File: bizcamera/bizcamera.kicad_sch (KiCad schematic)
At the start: 1 part

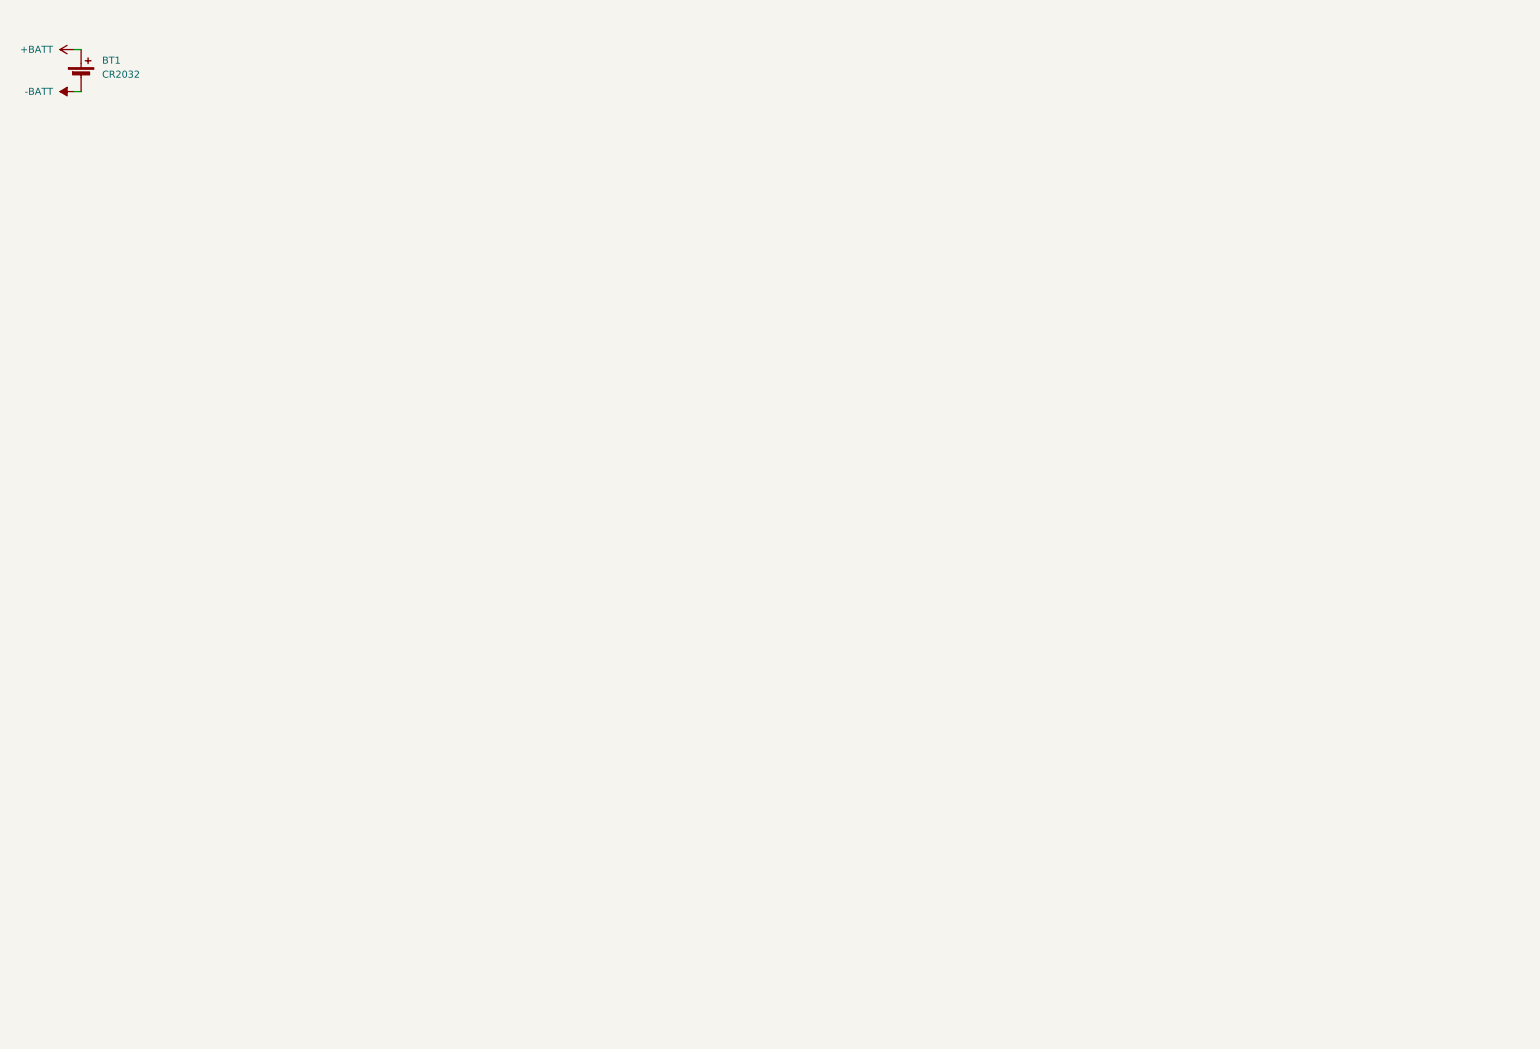
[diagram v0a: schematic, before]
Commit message: Schematic rev1
Rev1 of the schematic, not finished, but close.

Switched to rp2350 because PIO is powerful enough to grab frames without DCMI iface
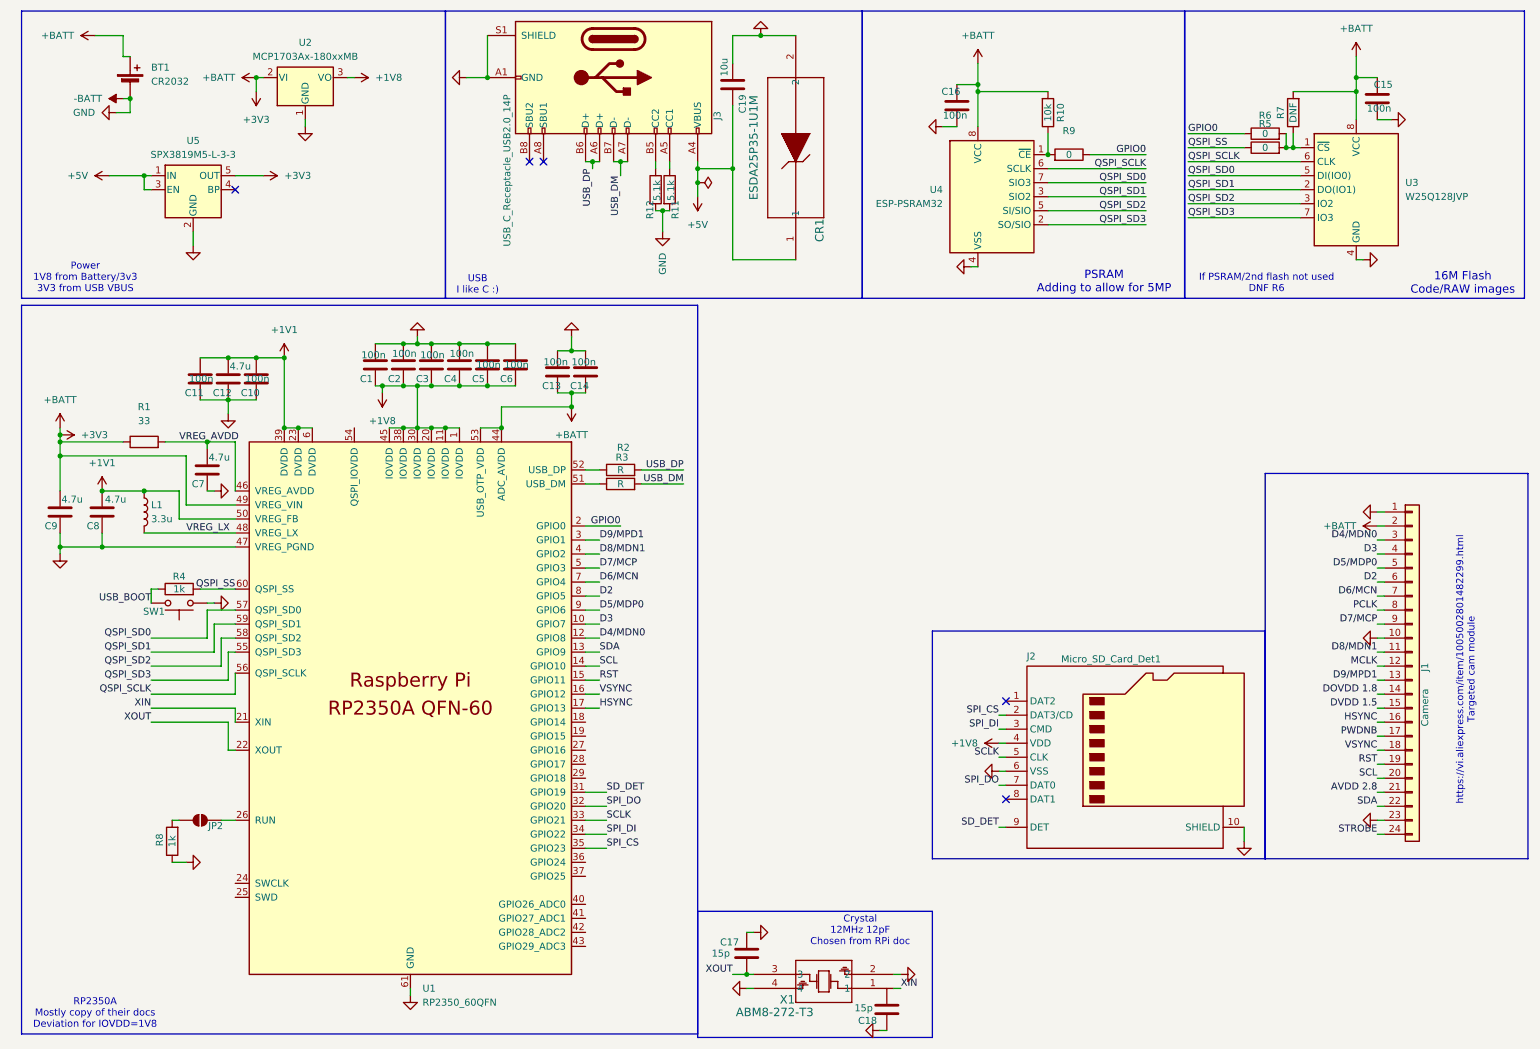
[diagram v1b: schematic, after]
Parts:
- added C1, C10, C11, C13, C14, C15, C16, C2, C3, C4, C5, C6: 100n, Capacitor_SMD:C_0402_1005Metric, symbol Device:C
- added C12, C7, C8, C9: 4.7u, Capacitor_SMD:C_0402_1005Metric, symbol Device:C
- added C17, C18: 15p, Capacitor_SMD:C_0402_1005Metric, symbol Device:C
- added C19: 10u, Capacitor_SMD:C_0603_1608Metric, symbol Device:C
- added CR1: ESDA25P35-1U1M, lib:QFN1610_STM-M, symbol ESDA25P35:ESDA25P35-1U1M
- added J1: Camera, Connector_FFC-FPC:Hirose_FH12-24S-0.5SH_1x24-1MP_P0.50mm_Horizontal, symbol Connector_Generic:Conn_01x24
- added J2: Micro_SD_Card_Det1, Connector_Card:microSD_HC_Hirose_DM3D-SF, symbol Connector:Micro_SD_Card_Det1
- added J3: USB_C_Receptacle_USB2.0_14P, Connector_USB:USB_C_Receptacle_HCTL_HC-TYPE-C-16P-01A, symbol Connector:USB_C_Receptacle_USB2.0_16P
- added JP2: USB_BOOT, Jumper:SolderJumper-2_P1.3mm_Open_RoundedPad1.0x1.5mm, symbol Jumper:SolderJumper_2_Open
- added L1: 3.3u, symbol Device:L
- added R1: 33, Resistor_SMD:R_0402_1005Metric, symbol Device:R
- added R10: 10k, Resistor_SMD:R_0402_1005Metric, symbol Device:R
- added R11, R12: 5.1k, Resistor_SMD:R_0603_1608Metric, symbol Device:R
- added R2, R3: R, Resistor_SMD:R_0402_1005Metric, symbol Device:R
- added R4, R8: 1k, Resistor_SMD:R_0402_1005Metric, symbol Device:R
- added R5, R6, R9: 0, Resistor_SMD:R_0402_1005Metric, symbol Device:R
- added R7: DNF, Resistor_SMD:R_0402_1005Metric, symbol Device:R
- added SW1: USB_BOOT, symbol Switch:SW_Push
- added U1: RP2350_60QFN, RP2350A:RP2350-QFN-60-1EP_7x7_P0.4mm_EP3.4x3.4mm_ThermalVias, symbol RP2350A:RP2350_60QFN
- added U2: MCP1703Ax-180xxMB, Package_TO_SOT_SMD:SOT-89-3, symbol Regulator_Linear:MCP1703Ax-180xxMB
- added U3: W25Q128JVP, Package_SON:WSON-8-1EP_6x5mm_P1.27mm_EP3.4x4.3mm, symbol Memory_Flash:W25Q128JVP
- added U4: ESP-PSRAM32, Package_SO:SOIC-8_3.9x4.9mm_P1.27mm, symbol Memory_RAM:ESP-PSRAM32
- added U5: SPX3819M5-L-3-3, Package_TO_SOT_SMD:SOT-23-5, symbol Regulator_Linear:SPX3819M5-L-3-3
- added X1: ABM8-272-T3, symbol ABM8-272-T3:ABM8-272-T3
- BT1: footprint (none) -> Battery:BatteryHolder_Keystone_3009_1x2450
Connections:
- net -BATT: now also C1.1, C10.2, C11.2, C12.2, C13.1, C14.1, C15.1, C16.1, C17.2, C18.2, C19.2, C2.1, C3.1, C4.1, C5.1, C6.1, C7.2, C8.2, C9.2, CR1.2, J1.1 (Pin_1), J1.10 (Pin_10), J1.23 (Pin_23), J2.10 (SHIELD), J2.6 (VSS), J3.A1 (GND), J3.A12 (GND), J3.B1 (GND), J3.B12 (GND), J3.S1 (SHIELD), R11.2, R12.2, R8.1, SW1.1, U1.47 (VREG_PGND), U1.61 (GND), U2.1 (GND), U3.4 (GND), U4.4 (VSS), U5.2 (GND), X1.2, X1.4
- net +BATT renamed +3V3
- net +3V3: now also C13.2, C14.2, C15.2, C16.2, C9.1, J1.2 (Pin_2), R1.1, R10.2, R7.2, U1.44 (ADC_AVDD), U1.49 (VREG_VIN), U1.53 (USB_OTP_VDD), U2.2 (VI), U3.8 (VCC), U4.8 (VCC), U5.5 (OUT)
- new net: R10.1, R9.2, U4.1 (~{CE})
- new net: R5.2, R6.2, R7.1, U3.1 (~{CS})
- new net: J3.A5 (CC1), R11.1
- new net: J3.B5 (CC2), R12.1
- new net: JP2.2 (B), R8.2
- new net: R3.1, U1.51 (USB_DM)
- new net: JP2.1 (A), U1.26 (RUN)
- new net: R2.1, U1.52 (USB_DP)
- new net +1V1: C10.1, C11.1, C12.1, C8.1, L1.1, U1.23 (DVDD), U1.39 (DVDD), U1.50 (VREG_FB), U1.6 (DVDD)
- new net +1V8: C1.2, C2.2, C3.2, C4.2, C5.2, C6.2, J2.4 (VDD), U1.1 (IOVDD), U1.11 (IOVDD), U1.20 (IOVDD), U1.30 (IOVDD), U1.38 (IOVDD), U1.45 (IOVDD), U2.3 (VO)
- new net +5V: C19.1, CR1.1, J3.A4 (VBUS), J3.A9 (VBUS), J3.B4 (VBUS), J3.B9 (VBUS), U5.1 (IN), U5.3 (EN)
- new net AVDD 2.8: J1.21 (Pin_21)
- new net D2: J1.6 (Pin_6), U1.8 (GPIO5)
- new net D3: J1.4 (Pin_4), U1.10 (GPIO7)
- new net D4/MDN0: J1.3 (Pin_3), U1.12 (GPIO8)
- new net D5/MDP0: J1.5 (Pin_5), U1.9 (GPIO6)
- new net D6/MCN: J1.7 (Pin_7), U1.7 (GPIO4)
- new net D7/MCP: J1.9 (Pin_9), U1.5 (GPIO3)
- new net D8/MDN1: J1.11 (Pin_11), U1.4 (GPIO2)
- new net D9/MPD1: J1.13 (Pin_13), U1.3 (GPIO1)
- new net DOVDD 1.8: J1.14 (Pin_14)
- new net DVDD 1.5: J1.15 (Pin_15)
- new net GPIO0: R6.1, R9.1, U1.2 (GPIO0)
- new net HSYNC: J1.16 (Pin_16), U1.17 (GPIO13)
- new net MCLK: J1.12 (Pin_12)
- new net PCLK: J1.8 (Pin_8)
- new net PWDNB: J1.17 (Pin_17)
- new net QSPI_SCLK: U1.56 (QSPI_SCLK), U3.6 (CLK), U4.6 (SCLK)
- new net QSPI_SD0: U1.57 (QSPI_SD0), U3.5 (DI(IO0)), U4.7 (SIO3)
- new net QSPI_SD1: U1.59 (QSPI_SD1), U3.2 (DO(IO1)), U4.3 (SIO2)
- new net QSPI_SD2: U1.58 (QSPI_SD2), U3.3 (IO2), U4.5 (SI/SIO)
- new net QSPI_SD3: U1.55 (QSPI_SD3), U3.7 (IO3), U4.2 (SO/SIO)
- new net QSPI_SS: R4.2, R5.1, U1.60 (QSPI_SS)
- new net RST: J1.19 (Pin_19), U1.15 (GPIO11)
- new net SCL: J1.20 (Pin_20), U1.14 (GPIO10)
- new net SCLK: J2.5 (CLK), U1.33 (GPIO21)
- new net SDA: J1.22 (Pin_22), U1.13 (GPIO9)
- new net SD_DET: J2.9 (DET), U1.31 (GPIO19)
- new net SPI_CS: J2.2 (DAT3/CD), U1.35 (GPIO23)
- new net SPI_DI: J2.3 (CMD), U1.34 (GPIO22)
- new net SPI_DO: J2.7 (DAT0), U1.32 (GPIO20)
- new net STROBE: J1.24 (Pin_24)
- new net USB_BOOT: R4.1, SW1.2
- new net USB_DM: J3.A7 (D-), J3.B7 (D-), R3.2
- new net USB_DP: J3.A6 (D+), J3.B6 (D+), R2.2
- new net VREG_AVDD: C7.1, R1.2, U1.46 (VREG_AVDD)
- new net VREG_LX: L1.2, U1.48 (VREG_LX)
- new net VSYNC: J1.18 (Pin_18), U1.16 (GPIO12)
- new net XIN: U1.21 (XIN), X1.1
- new net XOUT: C17.1, U1.22 (XOUT), X1.3
- no-connect marks 0 -> 5
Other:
- note added: "16M Flash Code/RAW images"
- note added: "Crystal 12MHz 12pF Chosen from RPi doc"
- note added: "If PSRAM/2nd flash not used DNF R6"
- note added: "PSRAM Adding to allow for 5MP"
- note added: "Power 1V8 from Battery/3v3 3V3 from USB VBUS"
- note added: "RP2350A Mostly copy of their docs Deviation for IOVDD=1V8"
- note added: "USB I like C :)"
- note added: "https://vi.aliexpress.com/item/1005002801482299.html Targeted cam module"
- moved on the sheet: BT1

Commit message: Finish schematic
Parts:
- removed CR1: ESDA25P35-1U1M, lib:QFN1610_STM-M, symbol ESDA25P35:ESDA25P35-1U1M
- added C20, C21, C22, C23: 10u, Capacitor_SMD:C_0603_1608Metric, symbol Device:C
- added C24, C25, C27, C28, C29: 100n, Capacitor_SMD:C_0402_1005Metric, symbol Device:C
- added C26: 15p, Capacitor_SMD:C_0402_1005Metric, symbol Device:C
- added D1: LED, LED_SMD:LED_0805_2012Metric_Pad1.15x1.40mm_HandSolder, symbol Device:LED
- added JP1: CAM_AF, Jumper:SolderJumper-2_P1.3mm_Open_RoundedPad1.0x1.5mm, symbol Jumper:SolderJumper_2_Open
- added JP3: DVDD_1V8, Jumper:SolderJumper-2_P1.3mm_Open_RoundedPad1.0x1.5mm, symbol Jumper:SolderJumper_2_Open
- added JP4: XTAL_JMP, Jumper:SolderJumper-2_P1.3mm_Open_RoundedPad1.0x1.5mm, symbol Jumper:SolderJumper_2_Open
- added R13, R14, R15, R16: 10K, Resistor_SMD:R_0603_1608Metric, symbol Adafruit OV5640 Breakout-eagle-import:microbuilder_RESISTOR_0603_NOOUT
- added R17: 1k, Resistor_SMD:R_0402_1005Metric, symbol Device:R
- added SW2: SW_SPDT, Button_Switch_THT:SW_Slide_SPDT_Angled_CK_OS102011MA1Q, symbol Switch:SW_SPDT
- added U6: USBLC6-2P6, Package_TO_SOT_SMD:SOT-666, symbol Power_Protection:USBLC6-2P6
- added Y1: SG-210STF 24.0ML0, Oscillator:Oscillator_SMD_SeikoEpson_SG210-4Pin_2.5x2.0mm, symbol Oscillator:SG-210STF
- C18: value 15p -> 12p
- J3: value USB_C_Receptacle_USB2.0_14P -> USB_IN
- L1: footprint (none) -> RP2350A:L_pol_2016
- R2, R3: value R -> 0
- R5: now not fitted
- R7: value DNF -> 10k
- SW1: footprint (none) -> Button_Switch_SMD:SW_Push_1P1T_NO_CK_KMR2
- X1: footprint (none) -> ABM8_272_T3:ABM8-272-T3_ABR
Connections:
- net DOVDD 1.8 is gone; now on net +1V8: J1.14 (Pin_14)
- net +1V8: now also C23.1, C24.1, C27.1, C28.2, JP3.1 (A), Y1.4 (Vcc)
- net +3V3: now also U1.54 (QSPI_IOVDD), C21.1, C22.1, C29.2, JP1.1 (A), R14.1, R15.1, R16.1, SW2.1 (A); no longer BT1.1 (+), J1.2 (Pin_2)
- net +5V: now also C19.2, C20.1, U6.5 (VBUS); no longer C19.1
- net -BATT: now also C19.1, JP2.2 (B), C20.2, C21.2, C22.2, C23.2, C24.2, C25.1, C26.1, C27.2, C28.1, C29.1, R13.1, R17.1, U6.2 (GND), Y1.2 (GND); no longer C19.2, R8.1
- net AVDD 2.8: now also C25.2
- net DVDD 1.5: now also JP3.2 (B)
- net PCLK: now also U1.18 (GPIO14), C26.2
- net PWDNB: now also R13.2
- net RST: now also R14.2
- net SCL: now also R15.2
- net SDA: now also R16.2
- net USB_DM: now also U6.3 (I/O2); no longer J3.A7 (D-), J3.B7 (D-), R3.2
- net USB_DP: now also R2.1, U1.52 (USB_DP), U6.1 (I/O1); no longer J3.A6 (D+), J3.B6 (D+)
- net XIN: now also C18.1
- net XOUT: now also JP4.1 (A)
- net at R8.2: now also JP2.1 (A); no longer JP2.2 (B)
- net USB_DN: now reaches R3.1, U1.51 (USB_DM)
- net USB_DN: now also R3.2
- net at U1.26 (RUN): now also R8.1; no longer JP2.1 (A)
- net XTAL_EN: now reaches U1.28 (GPIO17)
- net XTAL_EN: now also Y1.1 (~{ST})
- net at U1.36 (GPIO24): now also D1.2 (A)
- net MCLK renamed CAM_XTAL
- net CAM_XTAL: now also JP4.2 (B), Y1.3 (OUT)
- new net: D1.1 (K), R17.2
- new net: J3.A6 (D+), J3.B6 (D+), U6.6 (I/O1)
- new net: J3.A7 (D-), J3.B7 (D-), U6.4 (I/O2)
- new net: J1.2 (Pin_2), JP1.2 (B)
- new net: BT1.1 (+), SW2.2 (B)
- no-connect marks 5 -> 6
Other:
- note added: "24MHz for Camera"
- note added: "If PSRAM/2nd flash not used DNP R6 Else DNP R5"
- note removed: "If PSRAM/2nd flash not used DNF R6"
- company: (none) -> kiyoo.moe
- moved on the sheet: BT1, C15, C16, C17, C18, C19, J1, J2, J3, JP2, R10, R11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

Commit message: Near final design
Near final design for prototype model, for both schematic and PCB

Layout was an absolute nightmare. But I think this is the best I can do with the constraints, and it should look pretty nice too.
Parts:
- removed SW2: SW_SPDT, Button_Switch_THT:SW_Slide_SPDT_Angled_CK_OS102011MA1Q, symbol Switch:SW_SPDT
- added C30, C33, C34, C35: 10u, Capacitor_SMD:C_0603_1608Metric, symbol Device:C
- added C31, C32: 68u, Capacitor_SMD:C_0603_1608Metric, symbol Device:C
- added L2, L3: 1u, Kiyo:TFM201610ALMA, symbol Device:L
- added R18: 10k, Resistor_SMD:R_0402_1005Metric, symbol Device:R
- added R19: 453k, Resistor_SMD:R_0402_1005Metric_Pad0.72x0.64mm_HandSolder, symbol Device:R
- added SW3: Shutter, Button_Switch_SMD:SW_Push_1P1T_NO_6x6mm_H9.5mm, symbol Switch:SW_Push
- added U7: TPS61022, Package_DFN_QFN:Texas_RWU0007A_VQFN-7_2x2mm_P0.5mm, symbol Converter_DCDC:TPS61022
- added U8: TPS628437DRL, Package_TO_SOT_SMD:SOT-563, symbol Regulator_Switching:TPS628437DRL
- D1: footprint LED_SMD:LED_0805_2012Metric_Pad1.15x1.40mm_HandSolder -> LED_SMD:LED_1206_3216Metric_ReverseMount_Hole1.8x2.4mm
- R13, R14, R15, R16: symbol Adafruit OV5640 Breakout-eagle-import:microbuilder_RESISTOR_0603_NOOUT -> Device:R
- R5: now fitted
- R6: value 0 -> 100k; footprint Resistor_SMD:R_0402_1005Metric -> Resistor_SMD:R_0402_1005Metric_Pad0.72x0.64mm_HandSolder
- U2: value MCP1703Ax-180xxMB -> SPX3819M5-L-1-8; footprint Package_TO_SOT_SMD:SOT-89-3 -> Package_TO_SOT_SMD:SOT-23-5; symbol Regulator_Linear:MCP1703Ax-180xxMB -> Regulator_Linear:SPX3819M5-L-1-8
- U3: value W25Q128JVP -> S25FS128SDSNFI101
- U4: value ESP-PSRAM32 -> ESP-PSRAM64
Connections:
- net USB_DM is gone; now on net USB_DN: U6.3 (I/O2)
- net +1V8: now also C15.2, C16.2, R10.2, R7.2, U2.5 (OUT), U3.8 (VCC), U4.8 (VCC), C33.1, C34.1, L3.2, R18.1, U8.6 (VOS); no longer U2.3 (VO)
- net +3V3: now also C31.1, C32.1, R19.2, U7.3 (VOUT); no longer C15.2, C16.2, C22.1, R10.2, R7.2, U2.2 (VI), U3.8 (VCC), U4.8 (VCC)
- net +5V: now also C22.1, U2.1 (IN), U2.3 (EN)
- net -BATT: now also R6.1, U2.2 (GND), C30.1, C31.2, C32.2, C33.2, C34.2, C35.2, SW3.1, U7.1 (GND), U7.6 (MODE), U8.1 (GND), U8.3 (VSET); no longer U2.1 (GND)
- net D2: now also U1.7 (GPIO4); no longer U1.8 (GPIO5)
- net D3: now also U1.4 (GPIO2); no longer U1.10 (GPIO7)
- net D4/MDN0: now also U1.3 (GPIO1); no longer U1.12 (GPIO8)
- net D5/MDP0: now also U1.5 (GPIO3); no longer U1.9 (GPIO6)
- net D6/MCN: now also U1.8 (GPIO5); no longer U1.7 (GPIO4)
- net D7/MCP: now also U1.12 (GPIO8); no longer U1.5 (GPIO3)
- net D8/MDN1: now also U1.13 (GPIO9); no longer U1.4 (GPIO2)
- net D9/MPD1: now also U1.14 (GPIO10); no longer U1.3 (GPIO1)
- net GPIO0: no longer R6.1
- net HSYNC: now also U1.15 (GPIO11); no longer U1.17 (GPIO13)
- net PCLK: now also U1.9 (GPIO6); no longer U1.18 (GPIO14)
- net QSPI_SD0: now also U4.5 (SI/SIO); no longer U4.7 (SIO3)
- net QSPI_SD1: now also U4.2 (SO/SIO); no longer U4.3 (SIO2)
- net QSPI_SD2: now also U4.3 (SIO2); no longer U4.5 (SI/SIO)
- net QSPI_SD3: now also U4.7 (SIO3); no longer U4.2 (SO/SIO)
- net RST: now also U1.17 (GPIO13); no longer U1.15 (GPIO11)
- net SCL: now also U1.18 (GPIO14); no longer U1.14 (GPIO10)
- net SCLK: now also U1.32 (GPIO20); no longer U1.33 (GPIO21)
- net SDA: now also U1.19 (GPIO15); no longer U1.13 (GPIO9)
- net SD_DET: now also U1.35 (GPIO23); no longer U1.31 (GPIO19)
- net SPI_CS: now also U1.34 (GPIO22); no longer U1.35 (GPIO23)
- net SPI_DI: now also U1.33 (GPIO21); no longer U1.34 (GPIO22)
- net SPI_DO: now also U1.31 (GPIO19); no longer U1.32 (GPIO20)
- net USB_DN: now also J3.A7 (D-), J3.B7 (D-), U6.4 (I/O2)
- net USB_DP: now also J3.A6 (D+), J3.B6 (D+), U6.6 (I/O1)
- net at R5.2, R7.1, U3.1 (~{CS}): no longer R6.2
- net +BATT: now reaches BT1.1 (+)
- net +BATT: now also C30.2, C35.1, L2.1, U7.5 (EN), U7.7 (VIN), U8.2 (VIN), U8.4 (EN)
- net at U1.37 (GPIO25): now also R18.2, SW3.2
- new net: L2.2, U7.2 (SW)
- new net: R19.1, R6.2, U7.4 (FB)
- new net: L3.1, U8.5 (SW)
- no-connect marks 6 -> 7
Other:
- note added: "Power: CR2032/USB 1V8 from Battery/3v3 3V3 from USB VBUS"
- note removed: "Power 1V8 from Battery/3v3 3V3 from USB VBUS"
- moved on the sheet: BT1, C13, C14, C16, C20, C21, C22, C23, R10, R17, R9, U4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

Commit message: Tidy up
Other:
- moved on the sheet: BT1, C20, C21, C33, C34, C35, L3, U5, U8

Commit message: BOM and minor rework
I realised 68u 0603's were impossible lol
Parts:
- C1, C10, C11, C13, C14, C15, C16, C2, C24, C25, C27, C28, C29, C3, C4, C5, C6: LCSC (none) -> C1525
- C12, C7, C8, C9: LCSC (none) -> C76995
- C17, C26: LCSC (none) -> C1548
- C18: value 12p -> 15p; LCSC (none) -> C1548
- C19, C20, C21, C22, C23, C30, C33, C34, C35: LCSC (none) -> C1691
- C31, C32: LCSC (none) -> C7220
- D1: LCSC (none) -> C329183
- J1: LCSC (none) -> C202112
- J2: LCSC (none) -> C719027
- J3: LCSC (none) -> C2894897
- L2, L3: LCSC (none) -> C404808
- R1: LCSC (none) -> C25105
- R10, R18, R7: footprint Resistor_SMD:R_0402_1005Metric -> Resistor_SMD:R_0603_1608Metric; LCSC (none) -> C15401
- R11, R12: LCSC (none) -> C23186
- R13, R14, R15, R16: value 10K -> 10k; LCSC (none) -> C15401
- R17, R4, R8: LCSC (none) -> C11702
- R19: LCSC (none) -> C103049
- R2, R3, R5, R9: LCSC (none) -> C17168
- R6: LCSC (none) -> C25741
- SW1: LCSC (none) -> C72443
- SW3: LCSC (none) -> C22397173
- U1: LCSC (none) -> C42411118
- U2: LCSC (none) -> C18212663
- U3: LCSC (none) -> C2954241
- U5: LCSC (none) -> C5370980
- U6: LCSC (none) -> C2682291
- U7: LCSC (none) -> C915088
- U8: LCSC (none) -> C25838674
- X1: LCSC (none) -> C20625731
